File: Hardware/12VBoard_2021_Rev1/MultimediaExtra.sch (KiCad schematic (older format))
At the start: 29 parts, among them Q1 CSD18537NQ5A, Q2 CSD18531Q5A, U7 LM5116, U8 INA198

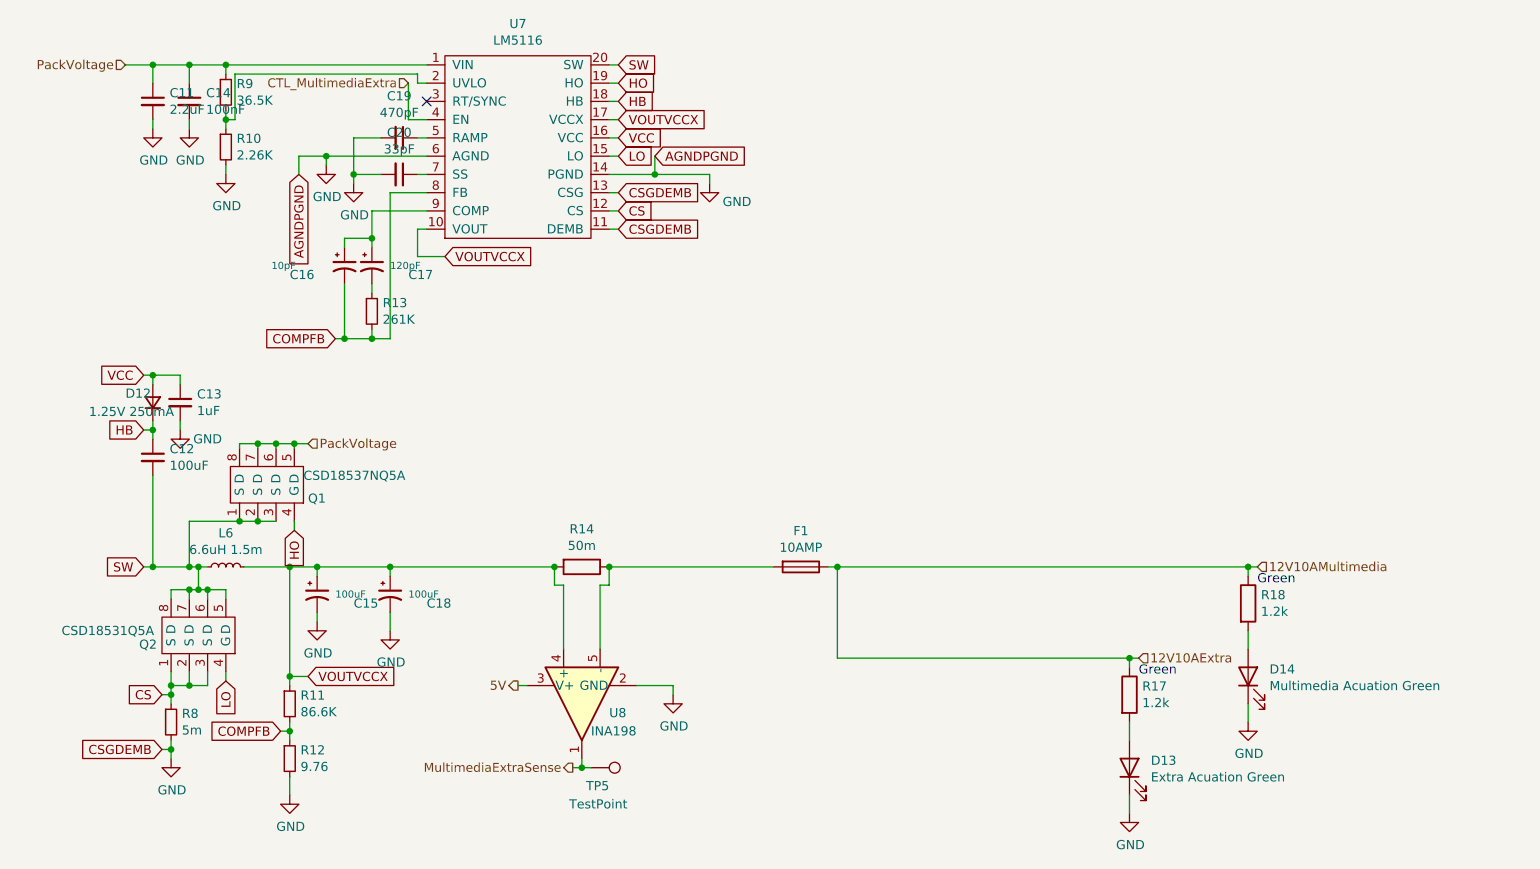
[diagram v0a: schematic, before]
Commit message: Changes!
Added the new correct connectors and redid all signal lines to the High Current side of the board. Also deleted all uncessacary components on the High current side that are no longer used.
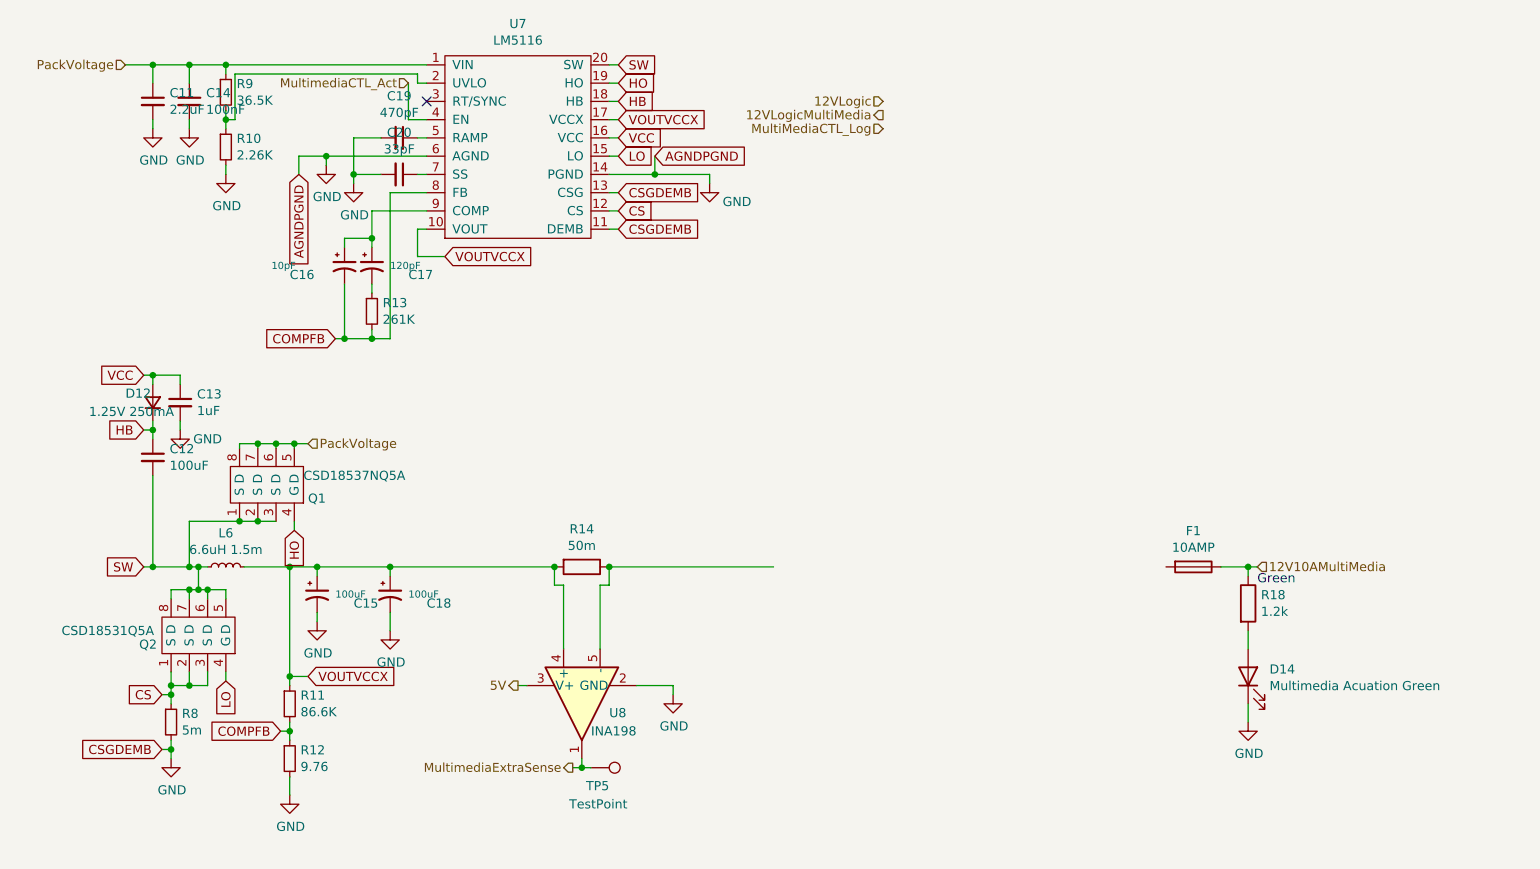
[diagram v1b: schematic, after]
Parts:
- removed D13: Extra Acuation Green, Diode_SMD:D_0603_1608Metric_Pad1.05x0.95mm_HandSolder, symbol Device:LED
- removed R17: 1.2k, Resistor_SMD:R_0603_1608Metric_Pad1.05x0.95mm_HandSolder, symbol Device:R
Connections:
- net at R14.1, U8.5 (-): no longer F1.2
- net 12V10AExtra renamed 12V10AMultiMedia
- net CTL_MultimediaExtra renamed MultimediaCTL_Act
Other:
- moved on the sheet: F1
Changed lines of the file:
@@
 $Descr A4 11693 8268
 encoding utf-8
-Sheet 6 8
+Sheet 6 9
 Title ""
 Date ""
@@
 Comment4 ""
 $EndDescr
-Wire Wire Line
-	4750 3550 4750 4050
-Wire Wire Line
-	4700 3550 4750 3550
-Connection ~ 4750 3550
-$Comp
-L Device:R R?
-U 1 1 5F945D14
-P 6350 4250
-AR Path="/5F74F36B/5F821EB2/5F945D14" Ref="R?"  Part="1"
-AR Path="/5F74F36B/5F8236F9/5F945D14" Ref="R17"  Part="1"
-F 0 "R17" H 6420 4296 50  0000 L CNN
-F 1 "1.2k" H 6420 4205 50  0000 L CNN
-F 2 "Resistor_SMD:R_0603_1608Metric_Pad1.05x0.95mm_HandSolder" V 6280 4250 50  0001 C CNN
-F 3 "~" H 6350 4250 50  0001 C CNN
-	1    6350 4250
-	1    0    0    -1
-$EndComp
-$Comp
-L power:GND #PWR?
-U 1 1 5F945D1A
-P 6350 4900
-AR Path="/5F74F36B/5F821EB2/5F945D1A" Ref="#PWR?"  Part="1"
-AR Path="/5F74F36B/5F8236F9/5F945D1A" Ref="#PWR052"  Part="1"
-F 0 "#PWR052" H 6350 4650 50  0001 C CNN
-F 1 "GND" H 6355 4727 50  0000 C CNN
-F 2 "" H 6350 4900 50  0001 C CNN
-F 3 "" H 6350 4900 50  0001 C CNN
-	1    6350 4900
-	1    0    0    -1
-$EndComp
-$Comp
-L Device:LED D?
-U 1 1 5F945D20
-P 6350 4650
-AR Path="/5F74F36B/5F821EB2/5F945D20" Ref="D?"  Part="1"
-AR Path="/5F74F36B/5F8236F9/5F945D20" Ref="D13"  Part="1"
-F 0 "D13" V 6389 4533 50  0000 R CNN
-F 1 "Extra Acuation Green" V 6298 4533 50  0000 R CNN
-F 2 "Diode_SMD:D_0603_1608Metric_Pad1.05x0.95mm_HandSolder" H 6350 4650 50  0001 C CNN
-F 3 "~" H 6350 4650 50  0001 C CNN
-	1    6350 4650
-	0    -1   -1   0
-$EndComp
-Wire Wire Line
-	6350 4900 6350 4800
-Wire Wire Line
-	6350 4500 6350 4400
-Wire Wire Line
-	6350 4100 6350 4050
 $Comp
 L Device:R R?
@@
 	7000 3600 7000 3550
 Wire Wire Line
-	4750 3550 7000 3550
-Wire Wire Line
 	7000 3550 7050 3550
-Connection ~ 7000 3550
-Text Notes 6400 4150 0    50   ~ 0
-Green
 Text Notes 7050 3650 0    50   ~ 0
 Green
@@
 L Device:Fuse F?
 U 1 1 5F92ED48
-P 4550 3550
+P 6700 3550
 AR Path="/5F74F36B/5F821EB2/5F92ED48" Ref="F?"  Part="1"
 AR Path="/5F74F36B/5F8236F9/5F92ED48" Ref="F1"  Part="1"
-F 0 "F1" V 4353 3550 50  0000 C CNN
-F 1 "10AMP" V 4444 3550 50  0000 C CNN
-F 2 "MRDT_Passives:ATC_Fuse_Block" V 4480 3550 50  0001 C CNN
-F 3 "~" H 4550 3550 50  0001 C CNN
-	1    4550 3550
+F 0 "F1" V 6503 3550 50  0000 C CNN
+F 1 "10AMP" V 6594 3550 50  0000 C CNN
+F 2 "MRDT_Passives:ATC_Fuse_Block" V 6630 3550 50  0001 C CNN
+F 3 "~" H 6700 3550 50  0001 C CNN
+	1    6700 3550
 	0    1    1    0
 $EndComp
 Text HLabel 3000 4200 0    50   Output ~ 0
 5V
-Text HLabel 6400 4050 2    50   Input ~ 0
-12V10AExtra
 Text HLabel 7050 3550 2    50   Input ~ 0
-12V10AMultimedia
-Wire Wire Line
-	6400 4050 6350 4050
-Connection ~ 6350 4050
+12V10AMultiMedia
 Text HLabel 3300 4650 0    49   Output ~ 0
 MultimediaExtraSense
@@
 $EndComp
 Text HLabel 2400 900  0    49   Input ~ 0
-CTL_MultimediaExtra
+MultimediaCTL_Act
 Text GLabel 3750 1300 2    50   Input ~ 0
 AGNDPGND
@@
 Text HLabel 1850 2875 2    50   Input ~ 0
 PackVoltage
-Wire Wire Line
-	4750 4050 6350 4050
+Text HLabel 5000 1000 0    50   Input ~ 0
+12VLogic
+Text HLabel 5000 1075 0    50   Output ~ 0
+12VLogicMultiMedia
+Wire Wire Line
+	6850 3550 7000 3550
+Connection ~ 7000 3550
+Text HLabel 5000 1150 0    50   Input ~ 0
+MultiMediaCTL_Log
 $EndSCHEMATC

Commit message: Added Mosfet cicuitry to turn on/off logic power for high current side
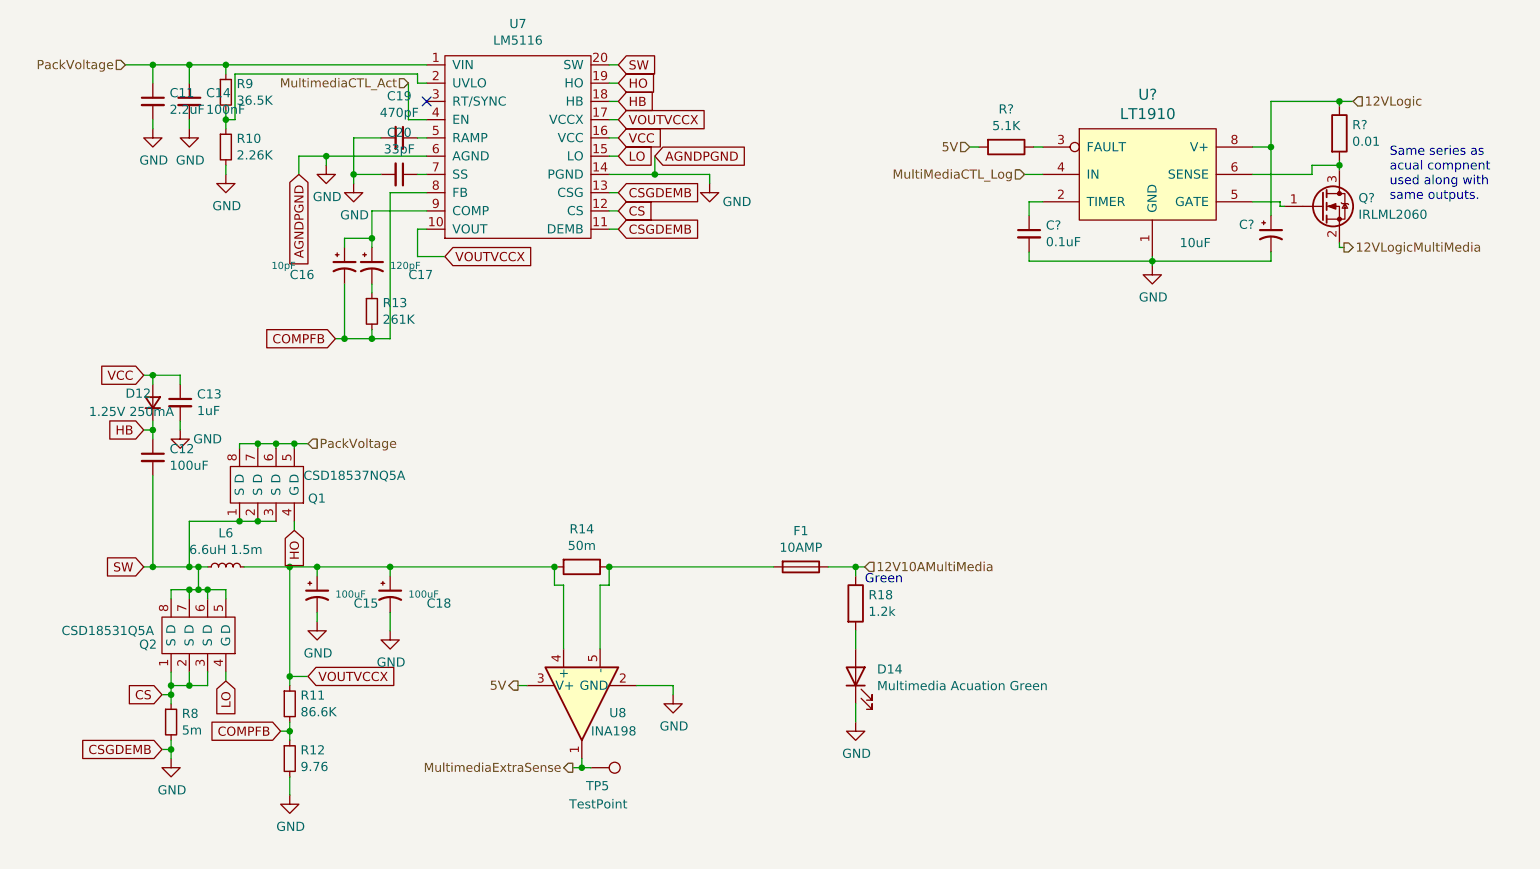
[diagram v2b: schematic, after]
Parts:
- added C?: 0.1uF, symbol Device:C_Small
- added C?: 10uF, symbol Device:CP1_Small
- added Q?: IRLML2060, Package_TO_SOT_SMD:SOT-23, symbol Transistor_FET:IRLML2060
- added R?: 0.01, symbol Device:R
- added R?: 5.1K, symbol Device:R
- added U?: LT1910, symbol MRDT_ICs:LT1910
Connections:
- net 12VLogic: now also C?.1, R?.1, U?.8 (V+)
- net 12VLogicMultiMedia: now also Q?.2 (S)
- net 5V: now also R?.2
- net GND: now also C?.2, C?.2, U?.1 (GND)
- net MultiMediaCTL_Log: now also U?.4 (IN)
- net at F1.2: now also R14.1, U8.5 (-)
- new net: C?.1, U?.2 (TIMER)
- new net: R?.1, U?.3 (FAULT)
- new net: Q?.1 (G), U?.5 (GATE)
- new net: Q?.3 (D), R?.2, U?.6 (SENSE)
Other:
- note added: "Same series as \nacual compnent\nused along with\nsame outputs."
- moved on the sheet: D14, F1, R18
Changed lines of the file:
@@
 L Device:R R?
 U 1 1 5F955B34
-P 7000 3750
+P 4850 3750
 AR Path="/5F74F36B/5F821EB2/5F955B34" Ref="R?"  Part="1"
 AR Path="/5F74F36B/5F8236F9/5F955B34" Ref="R18"  Part="1"
-F 0 "R18" H 7070 3796 50  0000 L CNN
-F 1 "1.2k" H 7070 3705 50  0000 L CNN
-F 2 "Resistor_SMD:R_0603_1608Metric_Pad1.05x0.95mm_HandSolder" V 6930 3750 50  0001 C CNN
-F 3 "~" H 7000 3750 50  0001 C CNN
-	1    7000 3750
+F 0 "R18" H 4920 3796 50  0000 L CNN
+F 1 "1.2k" H 4920 3705 50  0000 L CNN
+F 2 "Resistor_SMD:R_0603_1608Metric_Pad1.05x0.95mm_HandSolder" V 4780 3750 50  0001 C CNN
+F 3 "~" H 4850 3750 50  0001 C CNN
+	1    4850 3750
 	1    0    0    -1
 $EndComp
@@
 L power:GND #PWR?
 U 1 1 5F955B3A
-P 7000 4400
+P 4850 4400
 AR Path="/5F74F36B/5F821EB2/5F955B3A" Ref="#PWR?"  Part="1"
 AR Path="/5F74F36B/5F8236F9/5F955B3A" Ref="#PWR053"  Part="1"
-F 0 "#PWR053" H 7000 4150 50  0001 C CNN
-F 1 "GND" H 7005 4227 50  0000 C CNN
-F 2 "" H 7000 4400 50  0001 C CNN
-F 3 "" H 7000 4400 50  0001 C CNN
-	1    7000 4400
+F 0 "#PWR053" H 4850 4150 50  0001 C CNN
+F 1 "GND" H 4855 4227 50  0000 C CNN
+F 2 "" H 4850 4400 50  0001 C CNN
+F 3 "" H 4850 4400 50  0001 C CNN
+	1    4850 4400
 	1    0    0    -1
 $EndComp
@@
 L Device:LED D?
 U 1 1 5F955B40
-P 7000 4150
+P 4850 4150
 AR Path="/5F74F36B/5F821EB2/5F955B40" Ref="D?"  Part="1"
 AR Path="/5F74F36B/5F8236F9/5F955B40" Ref="D14"  Part="1"
-F 0 "D14" V 7039 4033 50  0000 R CNN
-F 1 "Multimedia Acuation Green" V 6948 4033 50  0000 R CNN
-F 2 "Diode_SMD:D_0603_1608Metric_Pad1.05x0.95mm_HandSolder" H 7000 4150 50  0001 C CNN
-F 3 "~" H 7000 4150 50  0001 C CNN
-	1    7000 4150
+F 0 "D14" V 4889 4033 50  0000 R CNN
+F 1 "Multimedia Acuation Green" V 4798 4033 50  0000 R CNN
+F 2 "Diode_SMD:D_0603_1608Metric_Pad1.05x0.95mm_HandSolder" H 4850 4150 50  0001 C CNN
+F 3 "~" H 4850 4150 50  0001 C CNN
+	1    4850 4150
 	0    -1   -1   0
 $EndComp
 Wire Wire Line
-	7000 4400 7000 4300
-Wire Wire Line
-	7000 3600 7000 3550
-Wire Wire Line
-	7000 3550 7050 3550
-Text Notes 7050 3650 0    50   ~ 0
+	4850 4400 4850 4300
+Wire Wire Line
+	4850 3600 4850 3550
+Wire Wire Line
+	4850 3550 4900 3550
+Text Notes 4900 3650 0    50   ~ 0
 Green
 $Comp
@@
 L Device:Fuse F?
 U 1 1 5F92ED48
-P 6700 3550
+P 4550 3550
 AR Path="/5F74F36B/5F821EB2/5F92ED48" Ref="F?"  Part="1"
 AR Path="/5F74F36B/5F8236F9/5F92ED48" Ref="F1"  Part="1"
-F 0 "F1" V 6503 3550 50  0000 C CNN
-F 1 "10AMP" V 6594 3550 50  0000 C CNN
-F 2 "MRDT_Passives:ATC_Fuse_Block" V 6630 3550 50  0001 C CNN
-F 3 "~" H 6700 3550 50  0001 C CNN
-	1    6700 3550
+F 0 "F1" V 4353 3550 50  0000 C CNN
+F 1 "10AMP" V 4444 3550 50  0000 C CNN
+F 2 "MRDT_Passives:ATC_Fuse_Block" V 4480 3550 50  0001 C CNN
+F 3 "~" H 4550 3550 50  0001 C CNN
+	1    4550 3550
 	0    1    1    0
 $EndComp
 Text HLabel 3000 4200 0    50   Output ~ 0
 5V
-Text HLabel 7050 3550 2    50   Input ~ 0
+Text HLabel 4900 3550 2    50   Input ~ 0
 12V10AMultiMedia
 Text HLabel 3300 4650 0    49   Output ~ 0
@@
 $EndComp
 Wire Wire Line
-	7000 3900 7000 4000
+	4850 3900 4850 4000
 $Comp
 L 12VBoard_2021_Rev1-rescue:CSD18531Q5A Q2
@@
 Text HLabel 1850 2875 2    50   Input ~ 0
 PackVoltage
-Text HLabel 5000 1000 0    50   Input ~ 0
+Text HLabel 7525 1800 2    50   Output ~ 0
+12VLogicMultiMedia
+Wire Wire Line
+	4700 3550 4850 3550
+Connection ~ 4850 3550
+Text HLabel 5775 1400 0    50   Input ~ 0
+MultiMediaCTL_Log
+Text HLabel 7575 1000 2    50   Input ~ 0
 12VLogic
-Text HLabel 5000 1075 0    50   Output ~ 0
-12VLogicMultiMedia
-Wire Wire Line
-	6850 3550 7000 3550
-Connection ~ 7000 3550
-Text HLabel 5000 1150 0    50   Input ~ 0
-MultiMediaCTL_Log
+$Comp
+L MRDT_ICs:LT1910 U?
+U 1 1 5FC479FB
+P 6075 1650
+AR Path="/5F74F36B/5F971CD6/5FC479FB" Ref="U?"  Part="1"
+AR Path="/5F74F36B/5F8236F9/5FC479FB" Ref="U?"  Part="1"
+F 0 "U?" H 6450 2337 60  0000 C CNN
+F 1 "LT1910" H 6450 2231 60  0000 C CNN
+F 2 "" H 6075 1650 60  0001 C CNN
+F 3 "" H 6075 1650 60  0001 C CNN
+	1    6075 1650
+	1    0    0    -1
+$EndComp
+$Comp
+L Device:C_Small C?
+U 1 1 5FC47A01
+P 5800 1725
+AR Path="/5F74F36B/5F971CD6/5FC47A01" Ref="C?"  Part="1"
+AR Path="/5F74F36B/5F8236F9/5FC47A01" Ref="C?"  Part="1"
+F 0 "C?" H 5892 1771 50  0000 L CNN
+F 1 "0.1uF" H 5892 1680 50  0000 L CNN
+F 2 "" H 5800 1725 50  0001 C CNN
+F 3 "~" H 5800 1725 50  0001 C CNN
+	1    5800 1725
+	1    0    0    -1
+$EndComp
+$Comp
+L Device:CP1_Small C?
+U 1 1 5FC47A07
+P 7125 1725
+AR Path="/5F74F36B/5F971CD6/5FC47A07" Ref="C?"  Part="1"
+AR Path="/5F74F36B/5F8236F9/5FC47A07" Ref="C?"  Part="1"
+F 0 "C?" H 6950 1775 50  0000 L CNN
+F 1 "10uF" H 6625 1675 50  0000 L CNN
+F 2 "" H 7125 1725 50  0001 C CNN
+F 3 "~" H 7125 1725 50  0001 C CNN
+	1    7125 1725
+	1    0    0    -1
+$EndComp
+$Comp
+L power:GND #PWR?
+U 1 1 5FC47A0D
+P 6475 1900
+AR Path="/5F74F36B/5F971CD6/5FC47A0D" Ref="#PWR?"  Part="1"
+AR Path="/5F74F36B/5F8236F9/5FC47A0D" Ref="#PWR?"  Part="1"
+F 0 "#PWR?" H 6475 1650 50  0001 C CNN
+F 1 "GND" H 6480 1727 50  0000 C CNN
+F 2 "" H 6475 1900 50  0001 C CNN
+F 3 "" H 6475 1900 50  0001 C CNN
+	1    6475 1900
+	1    0    0    -1
+$EndComp
+Wire Wire Line
+	6475 1850 6475 1875
+Wire Wire Line
+	6475 1900 6475 1875
+Connection ~ 6475 1875
+Wire Wire Line
+	6475 1875 5800 1875
+Wire Wire Line
+	5800 1875 5800 1825
+Wire Wire Line
+	7125 1825 7125 1875
+Wire Wire Line
+	6475 1875 7125 1875
+Wire Wire Line
+	7125 1625 7125 1250
+Wire Wire Line
+	7125 1250 7025 1250
+Wire Wire Line
+	5875 1550 5800 1550
+Wire Wire Line
+	5800 1550 5800 1625
+Wire Wire Line
+	5825 1250 5875 1250
+$Comp
+L Transistor_FET:IRLML2060 Q?
+U 1 1 5FC47A27
+P 7400 1575
+AR Path="/5F74F36B/5F971CD6/5FC47A27" Ref="Q?"  Part="1"
+AR Path="/5F74F36B/5F8236F9/5FC47A27" Ref="Q?"  Part="1"
+F 0 "Q?" H 7604 1621 50  0000 L CNN
+F 1 "IRLML2060" H 7604 1530 50  0000 L CNN
+F 2 "Package_TO_SOT_SMD:SOT-23" H 7600 1500 50  0001 L CIN
+F 3 "https://www.infineon.com/dgdl/irlml2060pbf.pdf?fileId=5546d462533600a401535664b7fb25ee" H 7400 1575 50  0001 L CNN
+	1    7400 1575
+	1    0    0    -1
+$EndComp
+Wire Wire Line
+	7025 1400 7350 1400
+Wire Wire Line
+	7350 1400 7350 1350
+Wire Wire Line
+	7350 1350 7500 1350
+Wire Wire Line
+	7500 1350 7500 1325
+Wire Wire Line
+	7500 1350 7500 1375
+Connection ~ 7500 1350
+Wire Wire Line
+	7125 1250 7125 1000
+Wire Wire Line
+	7125 1000 7500 1000
+Wire Wire Line
+	7500 1000 7500 1025
+Connection ~ 7125 1250
+Wire Wire Line
+	7525 1800 7500 1800
+Wire Wire Line
+	7500 1800 7500 1775
+Connection ~ 7500 1000
+Wire Wire Line
+	7500 1000 7575 1000
+Wire Wire Line
+	5775 1400 5875 1400
+Wire Wire Line
+	7200 1575 7175 1575
+Wire Wire Line
+	7175 1575 7175 1550
+Wire Wire Line
+	7175 1550 7025 1550
+Text Notes 7775 1550 0    50   ~ 0
+Same series as \nacual compnent\nused along with\nsame outputs.
+$Comp
+L Device:R R?
+U 1 1 5FC47A42
+P 7500 1175
+AR Path="/5F74F36B/5F971CD6/5FC47A42" Ref="R?"  Part="1"
+AR Path="/5F74F36B/5F8236F9/5FC47A42" Ref="R?"  Part="1"
+F 0 "R?" H 7570 1221 50  0000 L CNN
+F 1 "0.01" H 7570 1130 50  0000 L CNN
+F 2 "" V 7430 1175 50  0001 C CNN
+F 3 "~" H 7500 1175 50  0001 C CNN
+	1    7500 1175
+	1    0    0    -1
+$EndComp
+$Comp
+L Device:R R?
+U 1 1 5FC47A48
+P 5675 1250
+AR Path="/5F74F36B/5F971CD6/5FC47A48" Ref="R?"  Part="1"
+AR Path="/5F74F36B/5F8236F9/5FC47A48" Ref="R?"  Part="1"
+F 0 "R?" V 5468 1250 50  0000 C CNN
+F 1 "5.1K" V 5559 1250 50  0000 C CNN
+F 2 "" V 5605 1250 50  0001 C CNN
+F 3 "~" H 5675 1250 50  0001 C CNN
+	1    5675 1250
+	0    1    1    0
+$EndComp
+Text HLabel 5475 1250 0    50   Input ~ 0
+5V
+Wire Wire Line
+	5475 1250 5525 1250
 $EndSCHEMATC
